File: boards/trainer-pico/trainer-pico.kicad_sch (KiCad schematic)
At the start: 11 parts, among them J1 Conn_01x08_Pin, J10 Conn_01x04_Socket, J2 Conn_01x04_Pin, J3 Conn_01x06_Pin, J4 Conn_01x04_Pin, J5 Conn_01x04_Pin, J6 Conn_01x08_Socket, J7 Conn_01x04_Socket, J8 Conn_01x06_Socket, J9 Conn_01x04_Socket

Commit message: アノテーションの修正
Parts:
- renumbered J9 to J10, J5 to J4, J4 to J5, J10 to J9
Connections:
- net SPI_CS is gone; now on net +3.3V: J3.3 (Pin_3), J8.3 (Pin_3), U1.11 (UART1_RX/I2C0_SCL/SPI1_CSn/GP9)
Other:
- moved on the sheet: J10, J4, J5, J9

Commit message: 配線の取り回しを改善
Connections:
- net I2C_SCL: now also J4.3 (Pin_3), J9.3 (Pin_3); no longer J10.2 (Pin_2), J5.2 (Pin_2)
- net I2C_SDA: now also J4.2 (Pin_2), J9.2 (Pin_2); no longer J10.3 (Pin_3), J5.3 (Pin_3)
- net UART_PICO_RX: now also J10.2 (Pin_2), J5.2 (Pin_2); no longer J4.3 (Pin_3), J9.3 (Pin_3)
- net UART_PICO_TX: now also J10.3 (Pin_3), J5.3 (Pin_3); no longer J4.2 (Pin_2), J9.2 (Pin_2)
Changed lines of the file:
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@@
 	)
 	(label "I2C_SDA"
-		(at 146.05 142.24 0)
+		(at 146.05 124.46 0)
 		(effects
 			(font
@@
 	)
 	(label "UART_PICO_TX"
-		(at 146.05 124.46 0)
+		(at 146.05 142.24 0)
 		(effects
 			(font
@@
 	)
 	(label "I2C_SCL"
-		(at 146.05 139.7 0)
+		(at 146.05 127 0)
 		(effects
 			(font
@@
 	)
 	(label "UART_PICO_RX"
-		(at 146.05 127 0)
-		(effects
-			(font
+		(at 146.05 139.7 0)
+		(effects
+			(font

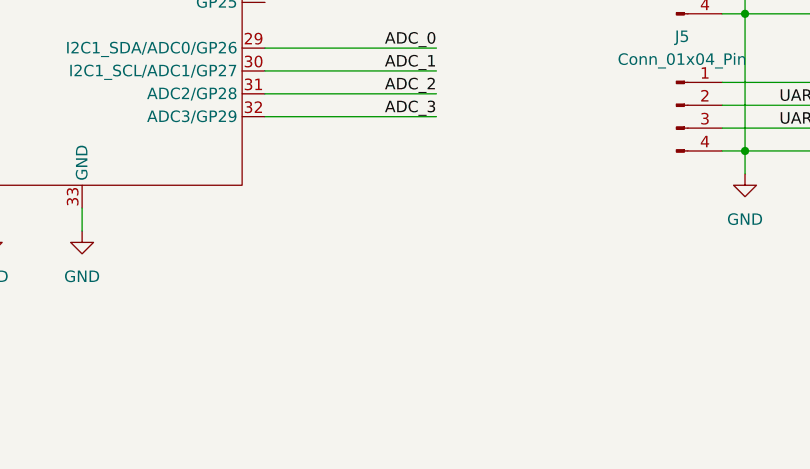
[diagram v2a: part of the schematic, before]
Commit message: I2C の外部プルアップ用の回路を追加
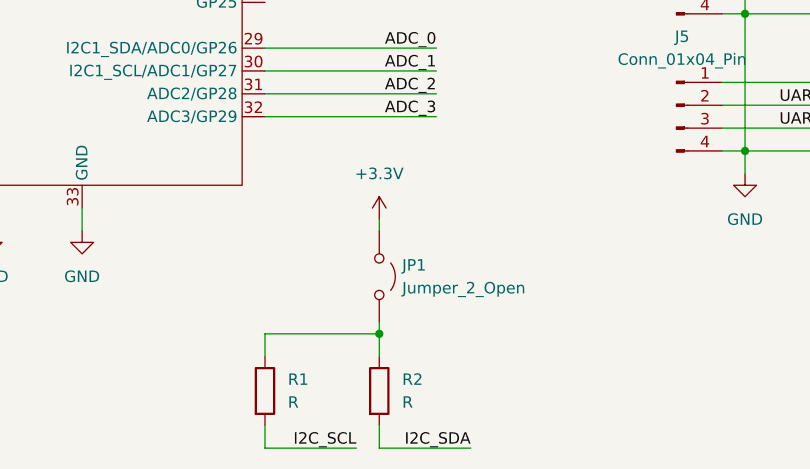
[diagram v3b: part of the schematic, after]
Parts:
- added JP1: Jumper_2_Open, Jumper:SolderJumper-2_P1.3mm_Open_RoundedPad1.0x1.5mm, symbol Jumper:Jumper_2_Open
- added R1, R2: R, Resistor_SMD:R_0603_1608Metric, symbol Device:R
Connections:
- net +3.3V: now also JP1.1 (A)
- net I2C_SCL: now also R1.2
- net I2C_SDA: now also R2.2
- new net: JP1.2 (B), R1.1, R2.1

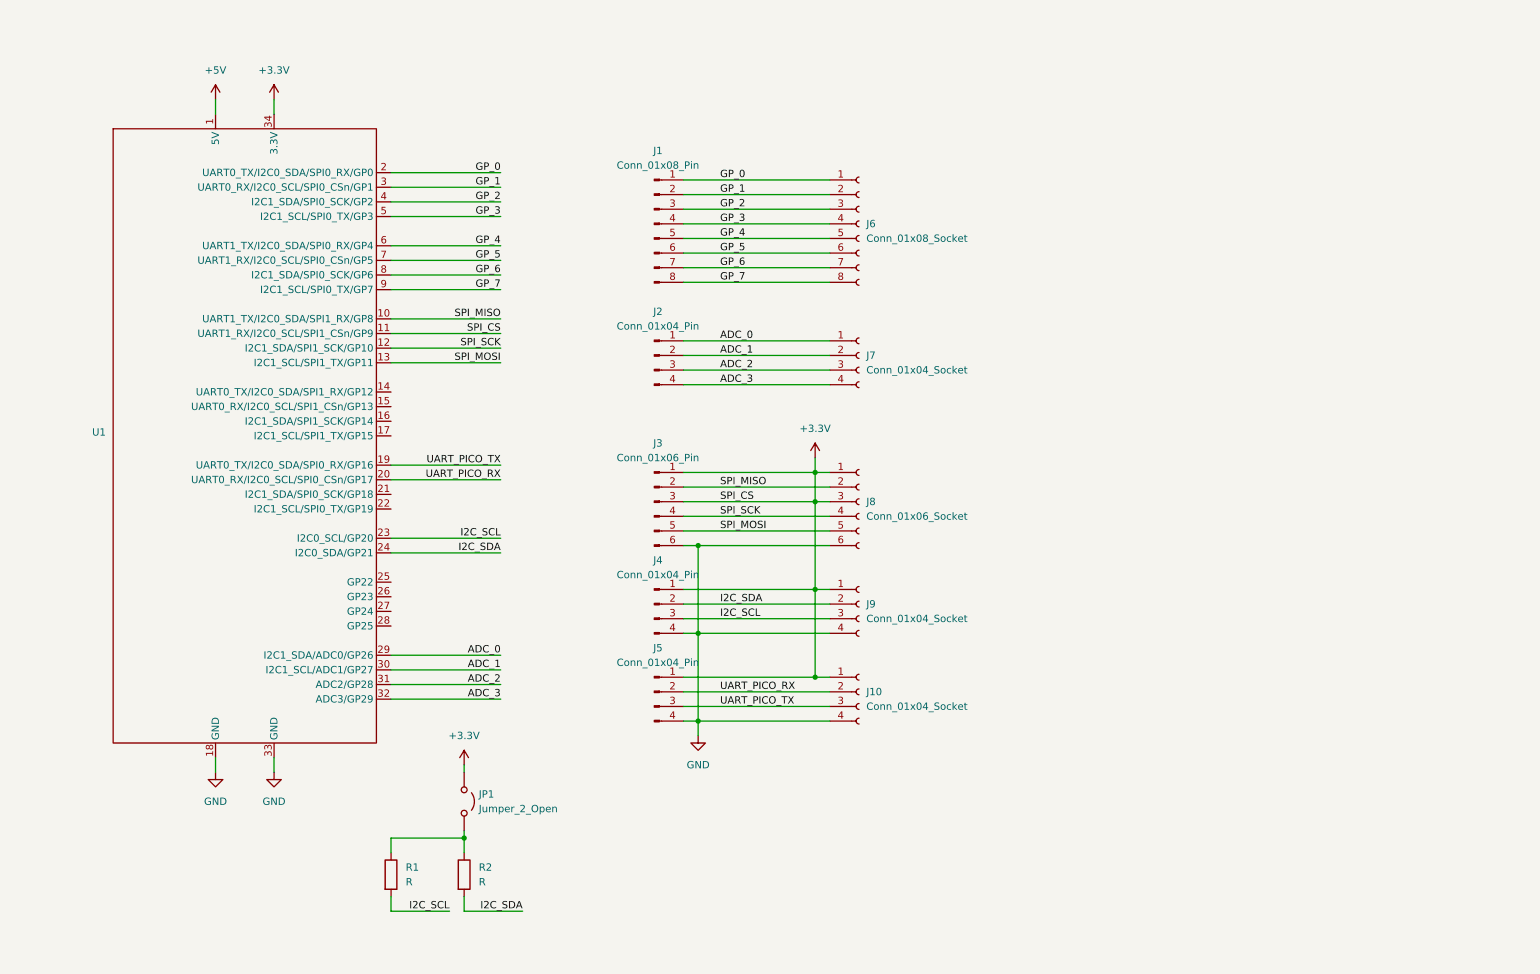
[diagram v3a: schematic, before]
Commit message: Pico の両側にピンソケット・ピンヘッダを追加
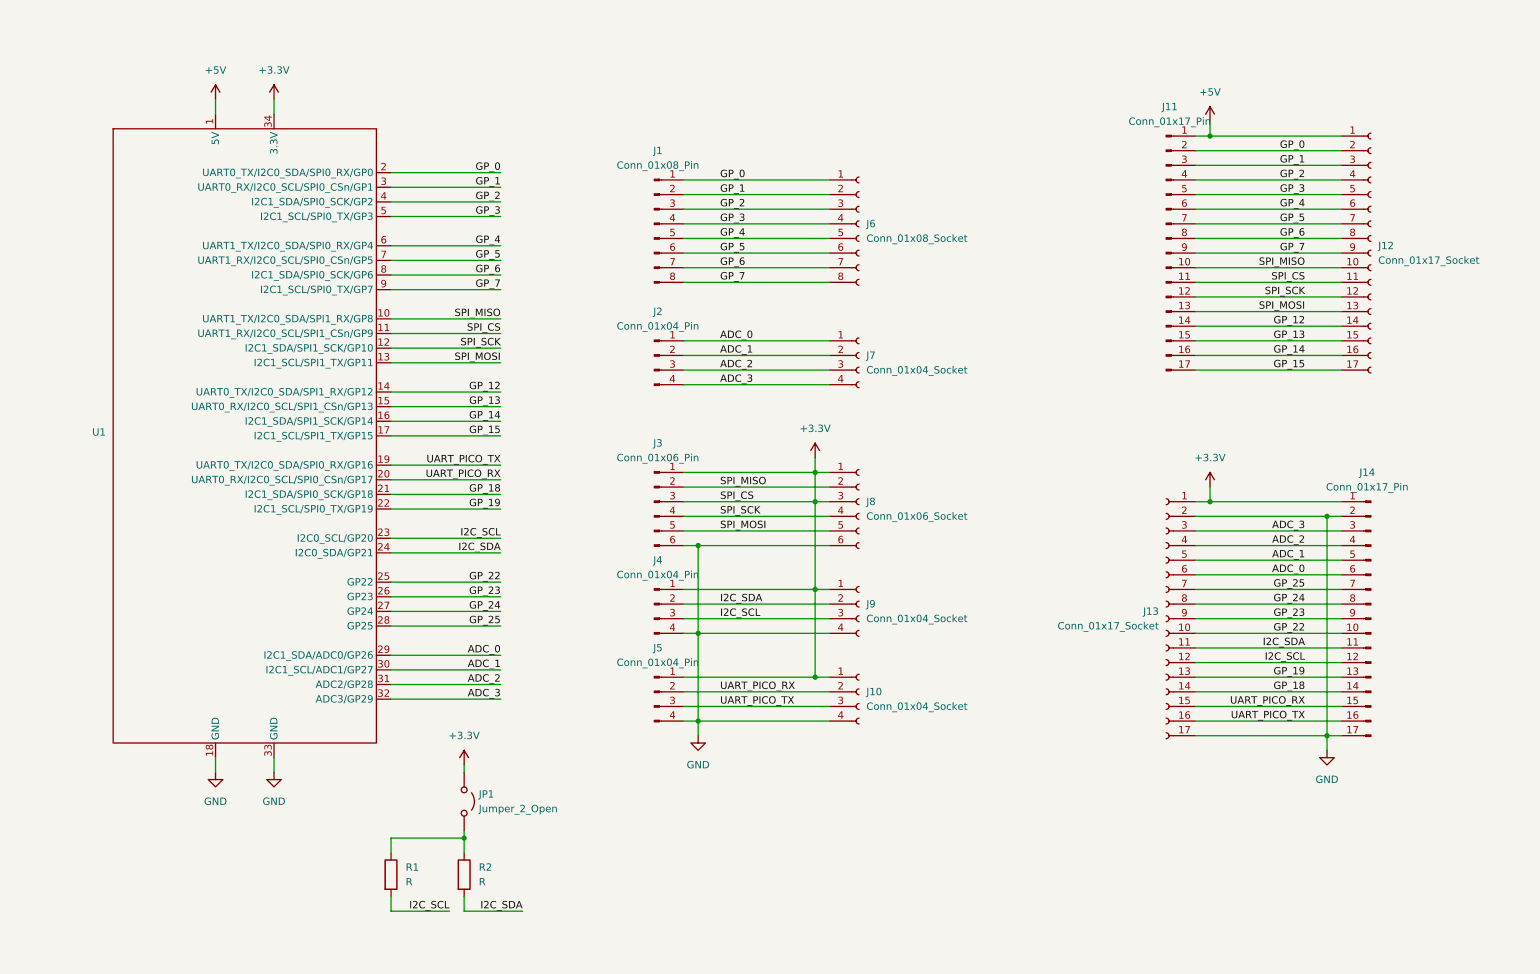
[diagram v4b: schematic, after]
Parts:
- added J11, J14: Conn_01x17_Pin, Connector_PinHeader_2.54mm:PinHeader_1x17_P2.54mm_Vertical, symbol Connector:Conn_01x17_Pin
- added J12, J13: Conn_01x17_Socket, Connector_PinSocket_2.54mm:PinSocket_1x17_P2.54mm_Vertical, symbol Connector:Conn_01x17_Socket
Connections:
- net +3.3V: now also J11.11 (Pin_11), J12.11 (Pin_11), J13.1 (Pin_1), J14.1 (Pin_1)
- net +5V: now also J11.1 (Pin_1), J12.1 (Pin_1)
- net ADC_0: now also J13.6 (Pin_6), J14.6 (Pin_6)
- net ADC_1: now also J13.5 (Pin_5), J14.5 (Pin_5)
- net ADC_2: now also J13.4 (Pin_4), J14.4 (Pin_4)
- net ADC_3: now also J13.3 (Pin_3), J14.3 (Pin_3)
- net GND: now also J13.17 (Pin_17), J13.2 (Pin_2), J14.17 (Pin_17), J14.2 (Pin_2)
- net GP_0: now also J11.2 (Pin_2), J12.2 (Pin_2)
- net GP_1: now also J11.3 (Pin_3), J12.3 (Pin_3)
- net GP_2: now also J11.4 (Pin_4), J12.4 (Pin_4)
- net GP_3: now also J11.5 (Pin_5), J12.5 (Pin_5)
- net GP_4: now also J11.6 (Pin_6), J12.6 (Pin_6)
- net GP_5: now also J11.7 (Pin_7), J12.7 (Pin_7)
- net GP_6: now also J11.8 (Pin_8), J12.8 (Pin_8)
- net GP_7: now also J11.9 (Pin_9), J12.9 (Pin_9)
- net I2C_SCL: now also J13.12 (Pin_12), J14.12 (Pin_12)
- net I2C_SDA: now also J13.11 (Pin_11), J14.11 (Pin_11)
- net SPI_MISO: now also J11.10 (Pin_10), J12.10 (Pin_10)
- net SPI_MOSI: now also J11.13 (Pin_13), J12.13 (Pin_13)
- net SPI_SCK: now also J11.12 (Pin_12), J12.12 (Pin_12)
- net UART_PICO_RX: now also J13.15 (Pin_15), J14.15 (Pin_15)
- net UART_PICO_TX: now also J13.16 (Pin_16), J14.16 (Pin_16)
- net GP_12: now reaches U1.14 (UART0_TX/I2C0_SDA/SPI1_RX/GP12)
- net GP_12: now also J11.14 (Pin_14), J12.14 (Pin_14)
- net GP_13: now reaches U1.15 (UART0_RX/I2C0_SCL/SPI1_CSn/GP13)
- net GP_13: now also J11.15 (Pin_15), J12.15 (Pin_15)
- net GP_14: now reaches U1.16 (I2C1_SDA/SPI1_SCK/GP14)
- net GP_14: now also J11.16 (Pin_16), J12.16 (Pin_16)
- net GP_15: now reaches U1.17 (I2C1_SCL/SPI1_TX/GP15)
- net GP_15: now also J11.17 (Pin_17), J12.17 (Pin_17)
- net GP_18: now reaches U1.21 (I2C1_SDA/SPI0_SCK/GP18)
- net GP_18: now also J13.14 (Pin_14), J14.14 (Pin_14)
- net GP_19: now reaches U1.22 (I2C1_SCL/SPI0_TX/GP19)
- net GP_19: now also J13.13 (Pin_13), J14.13 (Pin_13)
- net GP_22: now reaches U1.25 (GP22)
- net GP_22: now also J13.10 (Pin_10), J14.10 (Pin_10)
- net GP_23: now reaches U1.26 (GP23)
- net GP_23: now also J13.9 (Pin_9), J14.9 (Pin_9)
- net GP_24: now reaches U1.27 (GP24)
- net GP_24: now also J13.8 (Pin_8), J14.8 (Pin_8)
- net GP_25: now reaches U1.28 (GP25)
- net GP_25: now also J13.7 (Pin_7), J14.7 (Pin_7)

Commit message: 外部電源追加
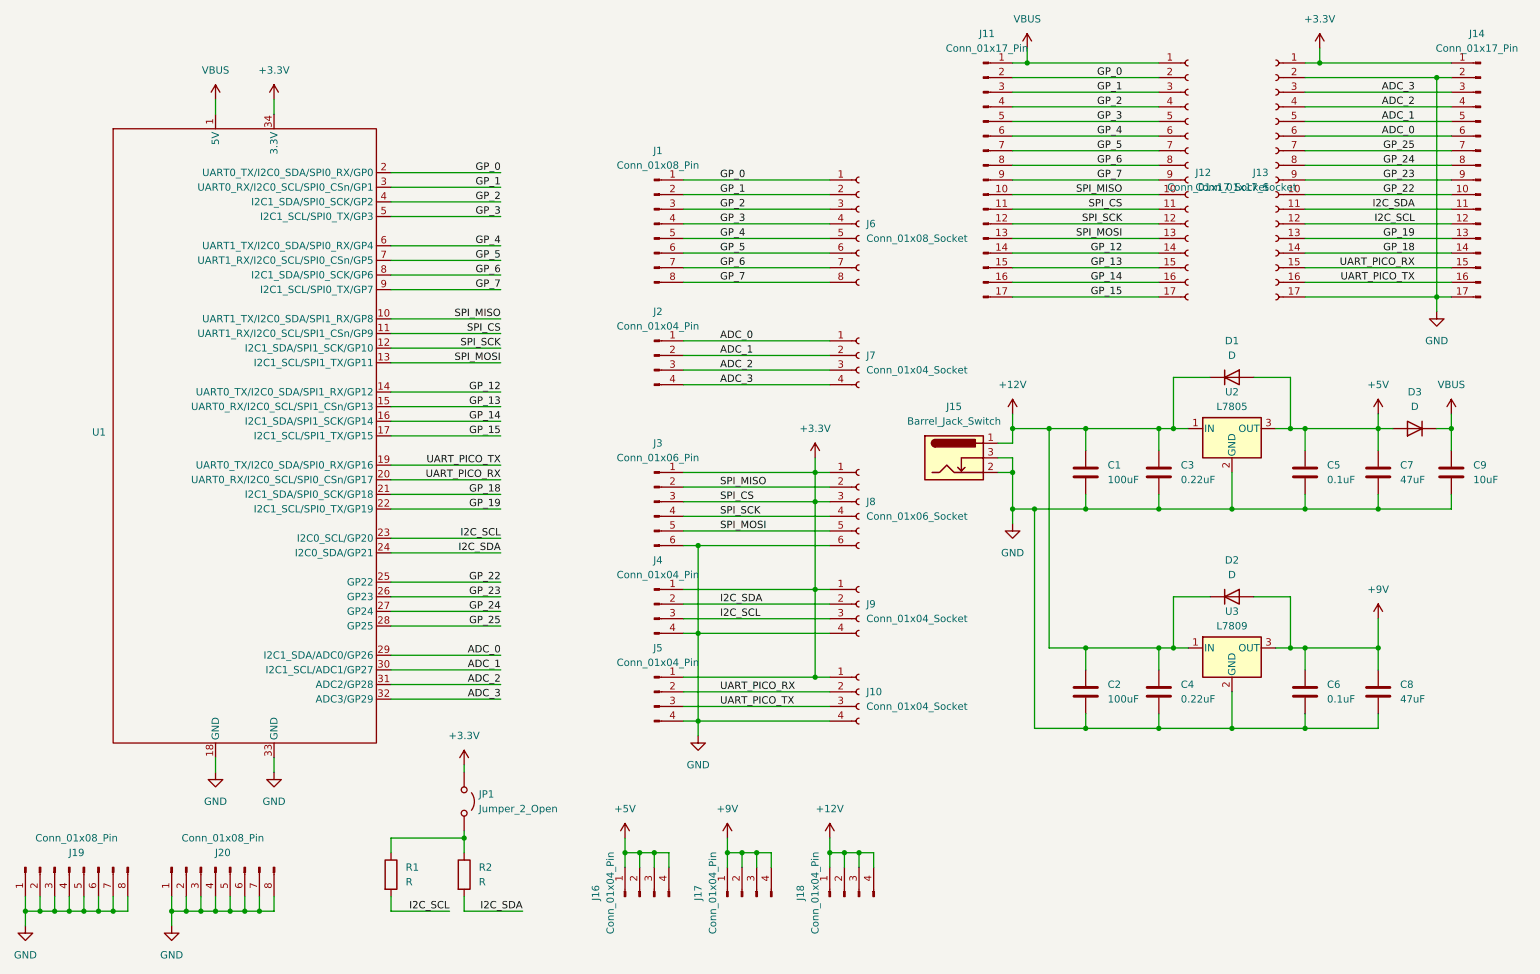
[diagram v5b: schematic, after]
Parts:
- added C1, C2: 100uF, Capacitor_THT:CP_Radial_D8.0mm_P3.50mm, symbol Device:C
- added C3, C4: 0.22uF, Capacitor_SMD:C_0805_2012Metric, symbol Device:C
- added C5, C6: 0.1uF, Capacitor_SMD:C_0603_1608Metric, symbol Device:C
- added C7, C8: 47uF, Capacitor_THT:CP_Radial_D6.3mm_P2.50mm, symbol Device:C
- added C9: 10uF, Capacitor_SMD:C_1206_3216Metric, symbol Device:C
- added D1, D2, D3: D, Diode_SMD:D_SOD-123F, symbol Device:D
- added J15: Barrel_Jack_Switch, Connector_BarrelJack:BarrelJack_Horizontal, symbol Connector:Barrel_Jack_Switch
- added J16, J17, J18: Conn_01x04_Pin, Connector_PinHeader_2.54mm:PinHeader_1x04_P2.54mm_Vertical, symbol Connector:Conn_01x04_Pin
- added J19, J20: Conn_01x08_Pin, Connector_PinHeader_2.54mm:PinHeader_1x08_P2.54mm_Vertical, symbol Connector:Conn_01x08_Pin
- added U2: L7805, Package_TO_SOT_SMD:TO-263-2, symbol Regulator_Linear:L7805
- added U3: L7809, Package_TO_SOT_SMD:TO-263-2, symbol Regulator_Linear:L7809
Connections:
- net +5V: now also C5.1, C7.1, D1.2 (A), D3.2 (A), J16.1 (Pin_1), J16.2 (Pin_2), J16.3 (Pin_3), J16.4 (Pin_4), U2.3 (OUT); no longer J11.1 (Pin_1), J12.1 (Pin_1), U1.1 (5V)
- net GND: now also C1.2, C2.2, C3.2, C4.2, C5.2, C6.2, C7.2, C8.2, C9.2, J15.2, J15.3, J19.1 (Pin_1), J19.2 (Pin_2), J19.3 (Pin_3), J19.4 (Pin_4), J19.5 (Pin_5), J19.6 (Pin_6), J19.7 (Pin_7), J19.8 (Pin_8), J20.1 (Pin_1), J20.2 (Pin_2), J20.3 (Pin_3), J20.4 (Pin_4), J20.5 (Pin_5), J20.6 (Pin_6), J20.7 (Pin_7), J20.8 (Pin_8), U2.2 (GND), U3.2 (GND)
- new net +12V: C1.1, C2.1, C3.1, C4.1, D1.1 (K), D2.1 (K), J15.1, J18.1 (Pin_1), J18.2 (Pin_2), J18.3 (Pin_3), J18.4 (Pin_4), U2.1 (IN), U3.1 (IN)
- new net +9V: C6.1, C8.1, D2.2 (A), J17.1 (Pin_1), J17.2 (Pin_2), J17.3 (Pin_3), J17.4 (Pin_4), U3.3 (OUT)
- new net VBUS: C9.1, D3.1 (K), J11.1 (Pin_1), J12.1 (Pin_1), U1.1 (5V)
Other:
- moved on the sheet: J11, J12, J13, J14

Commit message: PCBA 用のパーツ番号を追加
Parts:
- C3, C4: LCSC (none) -> C161262
- C5, C6: LCSC (none) -> C77055
- C9: LCSC (none) -> C77092
- D1, D2, D3: LCSC (none) -> C83528
- R1, R2: LCSC (none) -> C98220
- U2: LCSC (none) -> C86206
- U3: LCSC (none) -> C262905
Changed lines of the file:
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@@
 			)
 		)
+		(property "LCSC" "C83528"
+			(at 234.95 85.09 0)
+			(effects
+				(font
+					(size 1.27 1.27)
+				)
+				(hide yes)
+			)
+		)
 		(pin "2"
 		)
@@
 			)
 		)
+		(property "LCSC" "C262905"
+			(at 234.95 132.08 0)
+			(effects
+				(font
+					(size 1.27 1.27)
+				)
+				(hide yes)
+			)
+		)
 		(pin "1"
 		)
@@
 			)
 		)
+		(property "LCSC" "C83528"
+			(at 234.95 123.19 0)
+			(effects
+				(font
+					(size 1.27 1.27)
+				)
+				(hide yes)
+			)
+		)
 		(pin "2"
 		)
@@
 			)
 		)
+		(property "LCSC" "C86206"
+			(at 234.95 93.98 0)
+			(effects
+				(font
+					(size 1.27 1.27)
+				)
+				(hide yes)
+			)
+		)
 		(pin "1"
 		)
@@
 			)
 		)
+		(property "LCSC" "C98220"
+			(at 88.9 171.45 0)
+			(effects
+				(font
+					(size 1.27 1.27)
+				)
+				(hide yes)
+			)
+		)
 		(pin "1"
 		)
@@
 			)
 		)
+		(property "LCSC" "C161262"
+			(at 222.25 139.7 0)
+			(effects
+				(font
+					(size 1.27 1.27)
+				)
+				(hide yes)
+			)
+		)
 		(pin "1"
 		)
@@
 			)
 		)
+		(property "LCSC" "C77055"
+			(at 247.65 101.6 0)
+			(effects
+				(font
+					(size 1.27 1.27)
+				)
+				(hide yes)
+			)
+		)
 		(pin "1"
 		)
@@
 			)
 		)
+		(property "LCSC" "C161262"
+			(at 222.25 101.6 0)
+			(effects
+				(font
+					(size 1.27 1.27)
+				)
+				(hide yes)
+			)
+		)
 		(pin "1"
 		)
@@
 			)
 		)
+		(property "LCSC" "C77055"
+			(at 247.65 139.7 0)
+			(effects
+				(font
+					(size 1.27 1.27)
+				)
+				(hide yes)
+			)
+		)
 		(pin "1"
 		)
@@
 			)
 		)
+		(property "LCSC" "C98220"
+			(at 101.6 171.45 0)
+			(effects
+				(font
+					(size 1.27 1.27)
+				)
+				(hide yes)
+			)
+		)
 		(pin "1"
 		)
@@
 			)
 		)
+		(property "LCSC" "C83528"
+			(at 266.7 93.98 0)
+			(effects
+				(font
+					(size 1.27 1.27)
+				)
+				(hide yes)
+			)
+		)
 		(pin "2"
 		)
@@
 			(at 273.05 101.6 0)
 			(effects
+				(font
+					(size 1.27 1.27)
+				)
+				(hide yes)
+			)
+		)
+		(property "LCSC" "C77092"
+			(at 273.05 101.6 0)
+			(effects

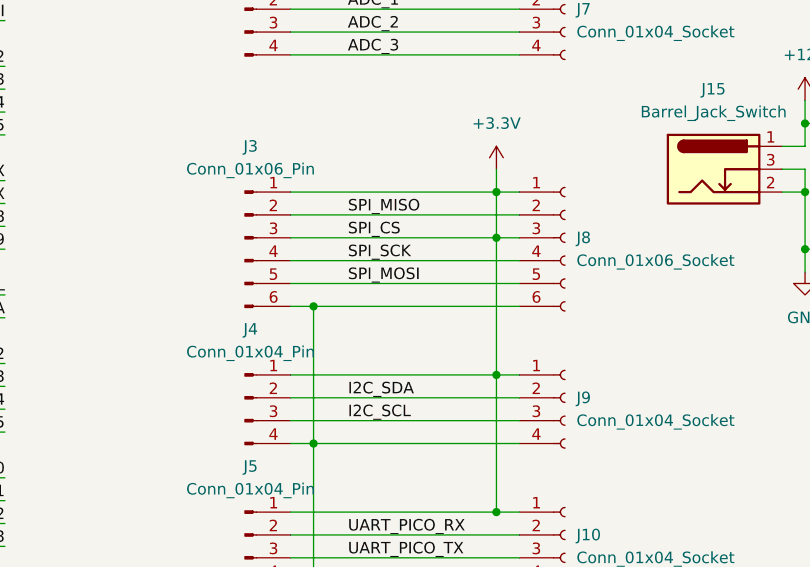
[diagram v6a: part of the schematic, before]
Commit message: ベタが気に食わなかったので修正
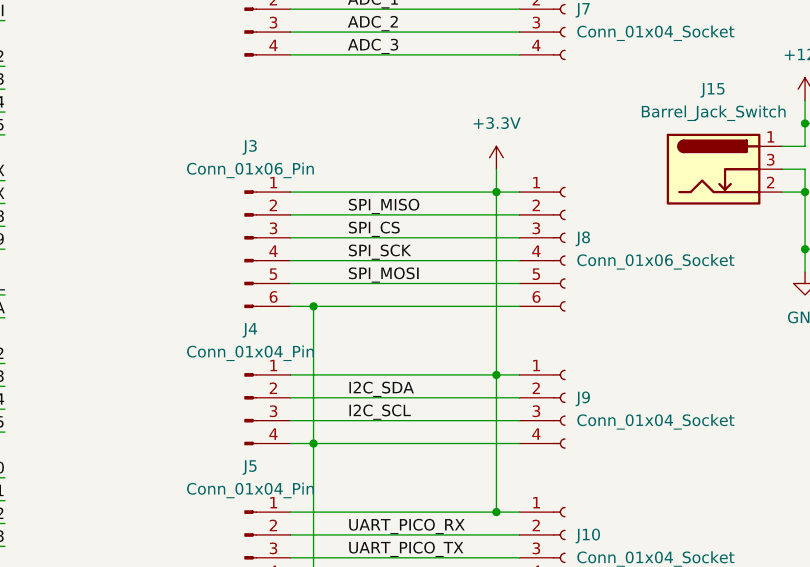
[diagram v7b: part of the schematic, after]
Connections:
- net +3.3V: no longer J11.11 (Pin_11), J12.11 (Pin_11), J3.3 (Pin_3), J8.3 (Pin_3), U1.11 (UART1_RX/I2C0_SCL/SPI1_CSn/GP9)
- new net SPI_CS: J11.11 (Pin_11), J12.11 (Pin_11), J3.3 (Pin_3), J8.3 (Pin_3), U1.11 (UART1_RX/I2C0_SCL/SPI1_CSn/GP9)
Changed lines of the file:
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@@
-	)
-	(junction
-		(at 162.56 106.68)
-		(diameter 0)
-		(color 0 0 0 0)
 	)
 	(junction
@@
 	(wire
 		(pts
-			(xy 162.56 106.68) (xy 165.1 106.68)
+			(xy 139.7 106.68) (xy 165.1 106.68)
 		)
 		(stroke
@@
 	(wire
 		(pts
-			(xy 162.56 101.6) (xy 162.56 106.68)
-		)
-		(stroke
-			(width 0)
-			(type default)
-		)
-	)
-	(wire
-		(pts
 			(xy 88.9 80.01) (xy 107.95 80.01)
 		)
@@
 	(wire
 		(pts
+			(xy 162.56 101.6) (xy 162.56 121.92)
+		)
+		(stroke
+			(width 0)
+			(type default)
+		)
+	)
+	(wire
+		(pts
 			(xy 209.55 107.95) (xy 222.25 107.95)
 		)
@@
 	(wire
 		(pts
-			(xy 162.56 106.68) (xy 162.56 121.92)
-		)
-		(stroke
-			(width 0)
-			(type default)
-		)
-	)
-	(wire
-		(pts
 			(xy 88.9 67.31) (xy 107.95 67.31)
 		)
@@
 		)
 		(stroke
-			(width 0)
-			(type default)
-		)
-	)
-	(wire
-		(pts
-			(xy 139.7 106.68) (xy 162.56 106.68)
-		)
-		(stroke

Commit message: ピンヘッダをピンソケットに変更
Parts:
- J16, J17, J18: footprint Connector_PinHeader_2.54mm:PinHeader_1x04_P2.54mm_Vertical -> Connector_PinSocket_2.54mm:PinSocket_1x04_P2.54mm_Vertical
- J19, J20: footprint Connector_PinHeader_2.54mm:PinHeader_1x08_P2.54mm_Vertical -> Connector_PinSocket_2.54mm:PinSocket_1x08_P2.54mm_Vertical
